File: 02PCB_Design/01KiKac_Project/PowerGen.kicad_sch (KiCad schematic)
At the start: 21 parts, among them J3 FCR7350R, J4 FCR7350R

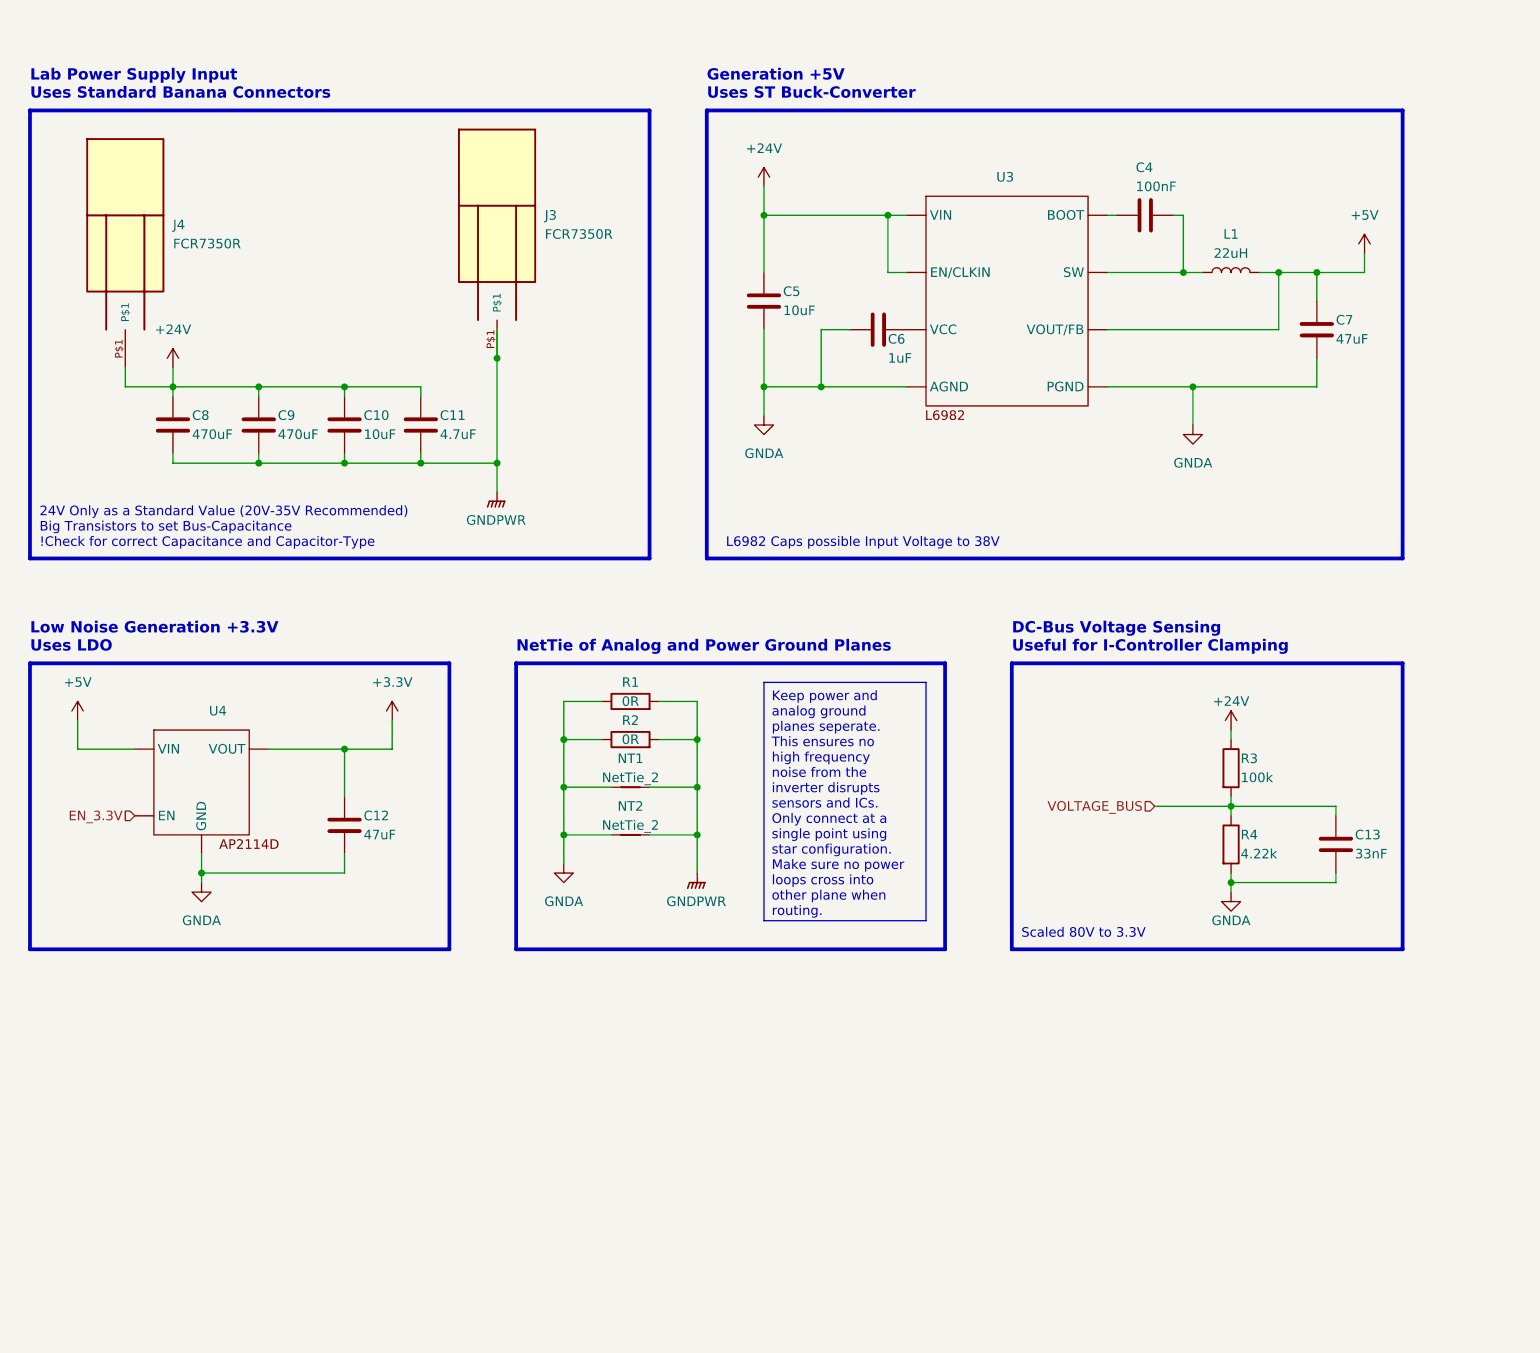
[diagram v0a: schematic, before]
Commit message: added CAN + minor changes
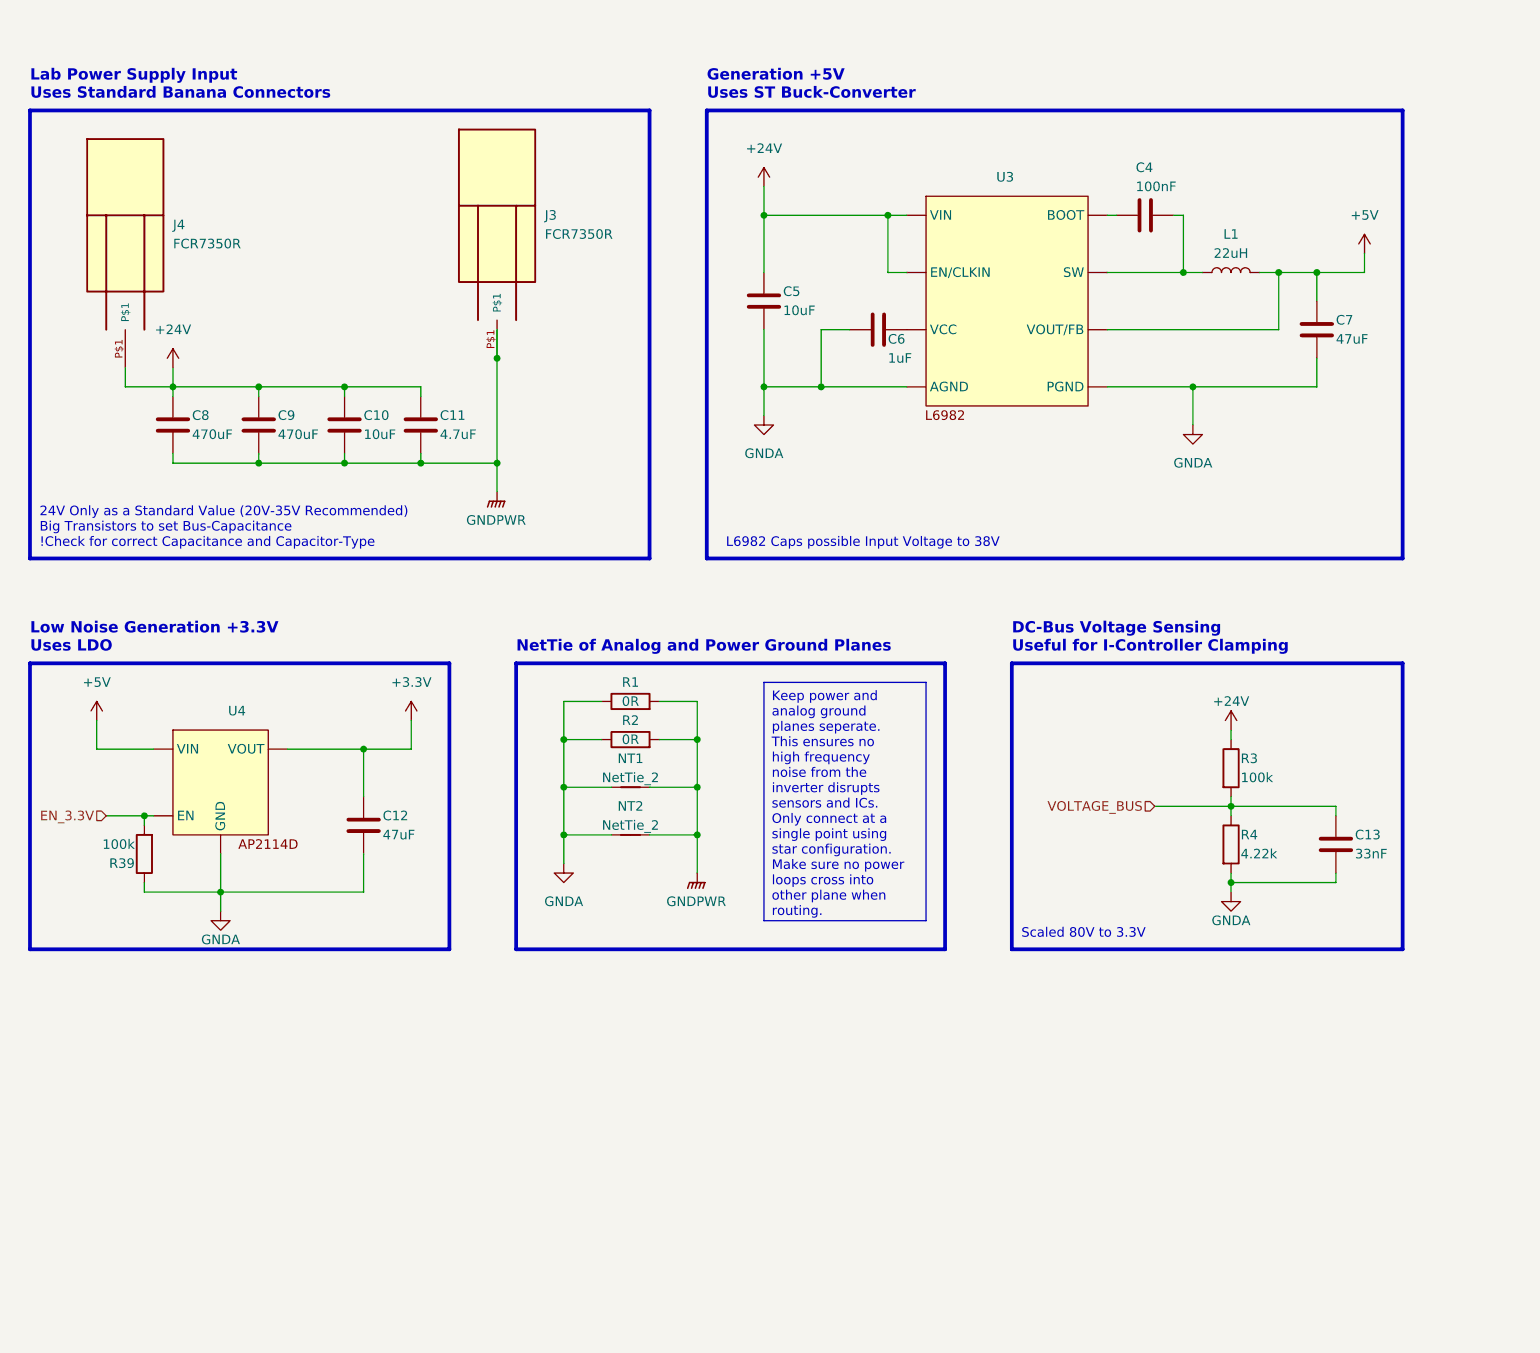
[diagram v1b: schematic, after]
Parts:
- added R39: 100k, Resistor_SMD:R_0402_1005Metric_Pad0.72x0.64mm_HandSolder, symbol Device:R
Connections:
- net EN_3.3V: now also R39.2
- net GNDA: now also R39.1
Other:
- moved on the sheet: C12

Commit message: cleanup
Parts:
- added C10, C11, C13: 10uF, Capacitor_THT:C_Axial_L5.1mm_D3.1mm_P7.50mm_Horizontal, symbol Device:C
- C8: now not fitted
- renumbered C10 to C12, C11 to C14, C12 to C15, C13 to C16, R1 to R5, R2 to R6, R3 to R7, R4 to R8, R39 to R9
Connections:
- net +24V: now also C10.1, C11.1, C13.1
- net GNDPWR: now also C10.2, C11.2, C13.2
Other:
- note added: "24V Only as a Standard Value (20V-35V Recommended) Big Capacitors to set Bus-Capacitance (514.7 uF)"
- note removed: "24V Only as a Standard Value (20V-35V Recommended) Big Transistors to set Bus-Capacitance !Check for correct Capacitance and Capacitor-Type"
- moved on the sheet: C12, C14, C15, C16, C4, C5, C6, C7, C9, J3, J4, L1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
